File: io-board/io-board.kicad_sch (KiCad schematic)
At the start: 18 parts, among them J5 Conn_01x24, U1 Littelfuse SP720, U2 Kamod BluePill STM32F103C8T6

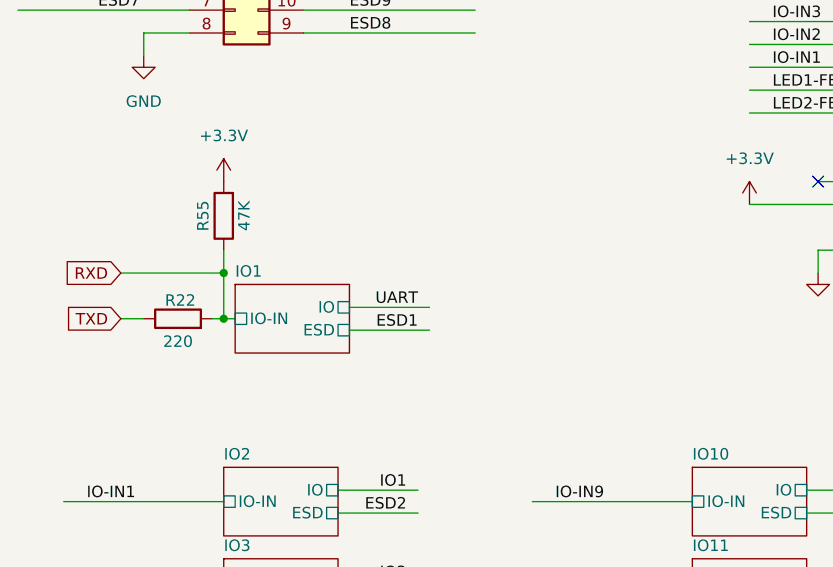
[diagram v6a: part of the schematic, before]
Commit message: New CAN-based physical layer, application protocol description, hi-res timers drafts.
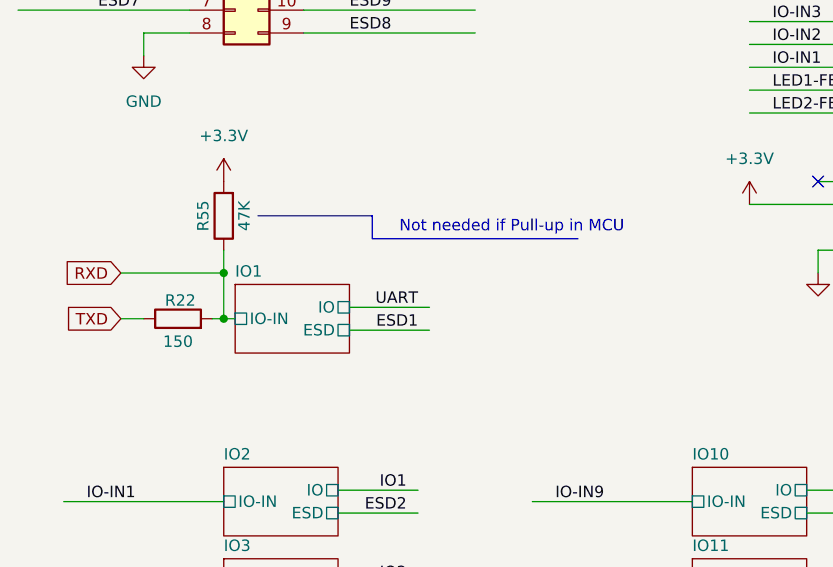
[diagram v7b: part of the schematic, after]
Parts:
- R22: value 220 -> 150
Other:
- note added: "Not needed if Pull-up in MCU"
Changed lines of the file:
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@@
 	(generator_version "9.0")
 	(paper "A4")
+	(text "Not needed if Pull-up in MCU"
+		(exclude_from_sim no)
+		(at 77.724 67.31 0)
+		(effects
+			(font
+				(size 1.27 1.27)
+			)
+		)
+	)
 	(junction
 		(at 45.72 77.47)
@@
 		)
 	)
+	(polyline
+		(pts
+			(xy 62.23 68.58) (xy 85.09 68.58)
+		)
+		(stroke
+			(width 0)
+			(type default)
+		)
+	)
 	(wire
 		(pts
@@
 		)
 	)
+	(polyline
+		(pts
+			(xy 49.53 66.04) (xy 62.23 66.04)
+		)
+		(stroke
+			(width 0)
+			(type default)
+		)
+	)
 	(wire
 		(pts
@@
 		)
 	)
+	(polyline
+		(pts
+			(xy 62.23 66.04) (xy 62.23 68.58)
+		)
+		(stroke
+			(width 0)
+			(type default)
+		)
+	)
 	(wire
 		(pts
@@
 			)
 		)
-		(property "Value" "220"
+		(property "Value" "150"
 			(at 40.64 80.01 90)
 			(effects
